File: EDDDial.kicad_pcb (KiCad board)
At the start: 2 copper layers, 49 parts, among them J1 USB_C_Receptacle_USB2.0_16P, J2 Conn_01x03_MountingPin, J3 Conn_ARM_SWD_TagConnect_TC203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, J4 Conn_01x05_MountingPin, J5 Conn_01x05_MountingPin, U1 nRF52820-QDxx, U3 WE-TVS-82400102, U4 TPS7A02DBV, U5 TMAG5173A1QDBVRQ1, U6 BQ24072RGT, Y1 32mhz, Y2 32.768khz

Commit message: primary design done, may change some minor things
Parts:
- removed C12, C15: 4.7uF, Capacitor_SMD:C_0402_1005Metric
- removed C14, C16, C18: 100nF, Capacitor_SMD:C_0402_1005Metric
- removed C17, C20: 1uF, Capacitor_SMD:C_0402_1005Metric
- removed C19: 100pF, Capacitor_SMD:C_0402_1005Metric
- removed C21: 47nF, Capacitor_SMD:C_0402_1005Metric
- removed C22: 1pF, Capacitor_SMD:C_0402_1005Metric
- removed C23: 1.2pF, Capacitor_SMD:C_0402_1005Metric
- removed D1: LED, LED_SMD:LED_0402_1005Metric
- removed L1: 10uH, Inductor_SMD:L_0402_1005Metric
- removed L2: 15nH, Inductor_SMD:L_0402_1005Metric
- removed L3: 4.7nF, Inductor_SMD:L_0402_1005Metric
- removed L4: 2.2nF, Inductor_SMD:L_0402_1005Metric
- removed U1: nRF52820-QDxx, Package_DFN_QFN:QFN-40-1EP_5x5mm_P0.4mm_EP3.6x3.6mm
- removed Y1: 32mhz, Crystal:Crystal_SMD_2012-2Pin_2.0x1.2mm
- added D2: LED, LED_SMD:LED_0402_1005Metric, F.Cu at (147.1, 52.5)
- added D3: LED, LED_SMD:LED_0402_1005Metric, F.Cu at (145.9, 54.5)
- added R11: 56k, Resistor_SMD:R_0402_1005Metric, F.Cu at (140.3, 40.2)
- added R12: 100k, Resistor_SMD:R_0402_1005Metric, F.Cu at (140.3, 42.2)
- added R13: 4.7k, Resistor_SMD:R_0402_1005Metric, F.Cu at (140.3, 44.2)
- added R14: 56k, Resistor_SMD:R_0402_1005Metric, F.Cu at (153.5, 46.3)
- added R8: 4.7k, Resistor_SMD:R_0402_1005Metric, F.Cu at (140.3, 38.3)
- added U2: MDBT50Q-1MV2, RF_Module:Raytac_MDBT50Q, F.Cu at (132.1, 46.0)
- C13: value 4.7uF -> 10uF
- C4: value 12pF -> 10uF
- C6: value 12pF -> 0.1uF
- C9: value 820pF -> 0.1uF
- R3: value 1.5k -> 10k
- moved C10 35.6 mm to (82.2, 77.8), turned to 180 degrees
- moved J4 34.5 mm to (82.5, 70.2), turned to 180 degrees
- moved Y2 32.1 mm to (129.1, 55.4), turned to 180 degrees
- moved U5 25.9 mm to (82.2, 75.6)
- moved J2 24.7 mm to (124.5, 70.7), turned to -90 degrees
- moved U6 23.8 mm to (117.0, 58.3)
- moved C6 23.2 mm to (135.1, 54.8)
- moved C7 20.0 mm to (127.1, 55.5), turned to 90 degrees
- moved C9 19.4 mm to (133.2, 54.8), turned to 180 degrees
- moved C4 19.1 mm to (133.2, 55.8)
- moved C8 18.5 mm to (131.1, 55.5), turned to 90 degrees
- moved C13 15.6 mm to (137.0, 54.8)
- moved R10 10.4 mm to (86.5, 43.6)
- moved R9 10.4 mm to (86.6, 41.6)
- moved U3 7.49 mm to (89.6, 42.6)
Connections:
- C2 pad 1: Net-(U4-VIN) -> Net-(SW1-A)
- C3 pad 1: Net-(U4-VIN) -> Net-(SW1-A)
- C4 pad 1: GND -> +3V3
- C4 pad 2: Net-(U1-XC1) -> GND
- C6 pad 1: GND -> +3V3
- C6 pad 2: Net-(U1-XC2) -> GND
- C9 pad 1: GND -> +3V3
- C9 pad 2: Net-(U1-DEC5) -> GND
- J3 pad 6: unconnected-(J3-SWO-Pad6) -> /SWO
- R3 pad 1: Net-(U4-VIN) -> Net-(SW1-B)
- R3 pad 2: Net-(D1-A) -> /CHG
- U4 pad 1: Net-(U4-VIN) -> Net-(SW1-A)
- U4 pad 3: Net-(U4-VIN) -> Net-(SW1-A)
- U6 pad 10: Net-(U4-VIN) -> Net-(SW1-B)
- U6 pad 11: Net-(U4-VIN) -> Net-(SW1-B)
- U6 pad 9: Net-(D1-K) -> /CHG
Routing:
- net VCC: track 0.00 -> 7.02 mm
- net /INT1: track 0.00 -> 5.51 mm, vias 0 -> 2
- net /SDA1: track 0.00 -> 2.82 mm
- net /SCL1: track 0.00 -> 2.66 mm
- net Net-(R10-Pad2): track 0.00 -> 1.49 mm
- net Net-(R9-Pad2): track 0.00 -> 1.37 mm
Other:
- copper layers 2 -> 4

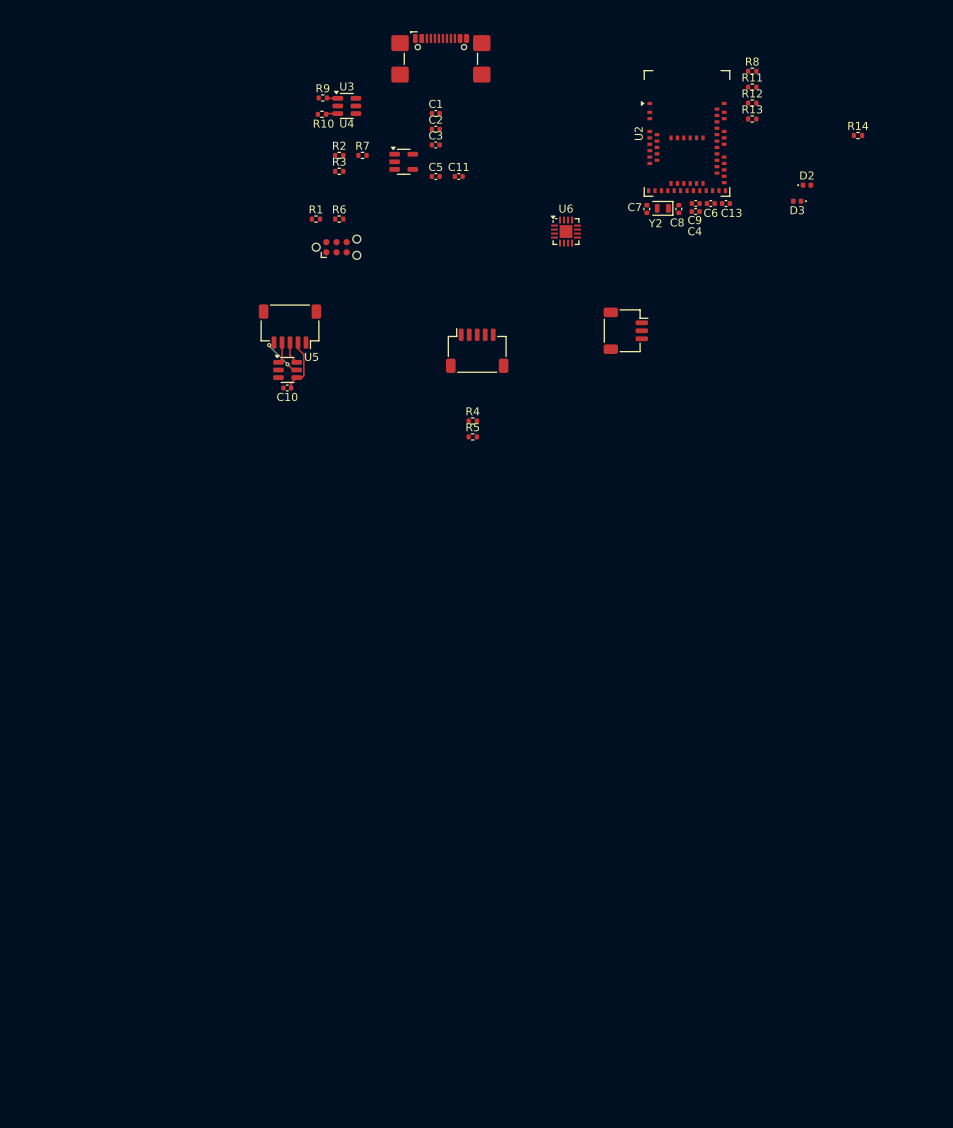
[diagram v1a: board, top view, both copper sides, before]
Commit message: Updated to be 60mm dia and completed basic routing
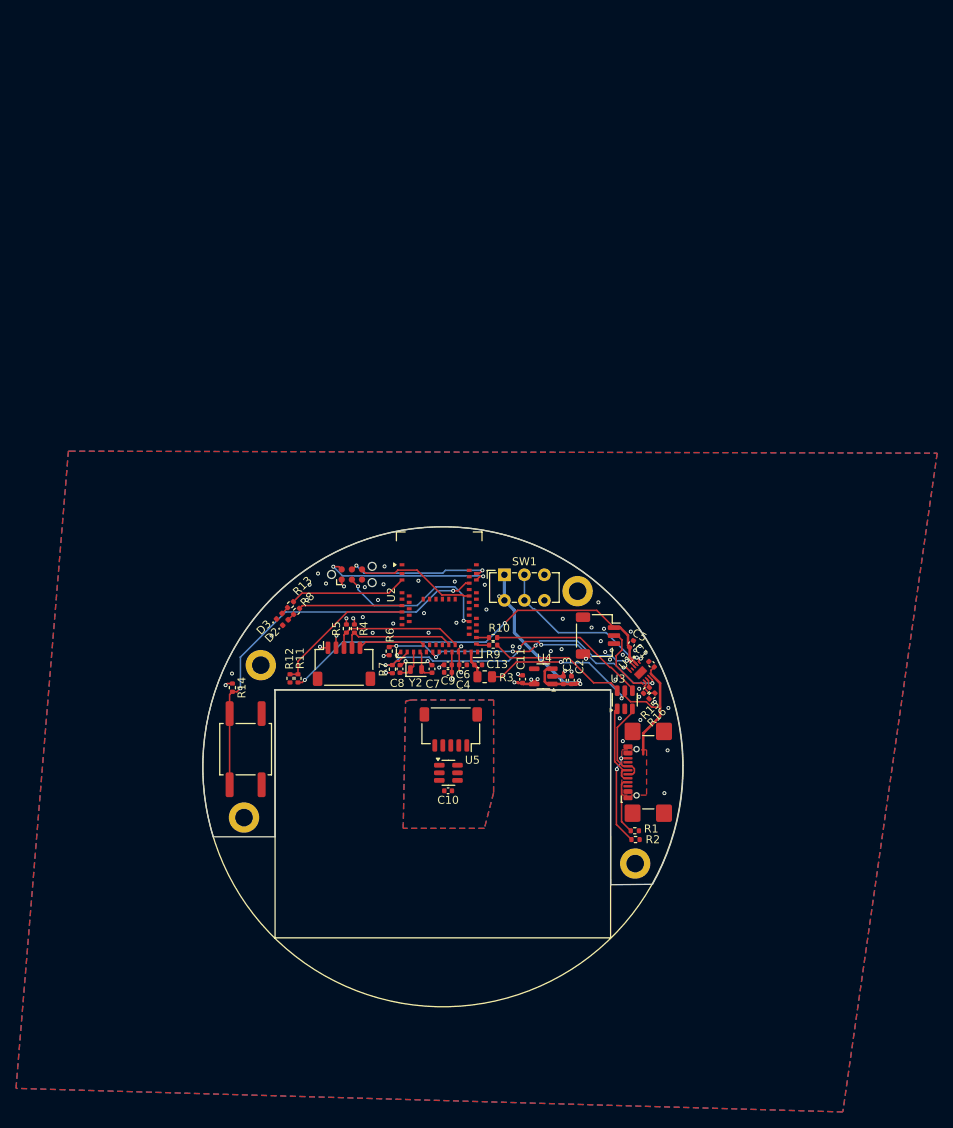
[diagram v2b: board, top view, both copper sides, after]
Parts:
- removed U6: BQ24072RGT, Package_DFN_QFN:VQFN-16-1EP_3x3mm_P0.5mm_EP1.6x1.6mm
- added H1: MountingHole_Pad, MountingHole:MountingHole_2.2mm_M2_DIN965_Pad, F.Cu at (78.8, 112.5)
- added H2: MountingHole_Pad, MountingHole:MountingHole_2.2mm_M2_DIN965_Pad, F.Cu at (76.8, 131.6)
- added H3: MountingHole_Pad, MountingHole:MountingHole_2.2mm_M2_DIN965_Pad, F.Cu at (118.5, 103.2)
- added H4: MountingHole_Pad, MountingHole:MountingHole_2.2mm_M2_DIN965_Pad, F.Cu at (125.7, 137.3)
- added R15: 1.2k, Resistor_SMD:R_0402_1005Metric, F.Cu at (127.0, 115.7)
- added R16: 18k, Resistor_SMD:R_0402_1005Metric, F.Cu at (127.8, 116.3)
- added SW1: SW_SPDT, Button_Switch_THT:SW_E-Switch_EG1271_SPDT, F.Cu at (109.3, 101.2)
- added SW2: SW_Push, Button_Switch_SMD:SW_Push_1P1T_NO_CK_KSC6xxG, F.Cu at (77.0, 123.0)
- added U1: BQ25185DLHR, FCU2025Lib:IC_BQ25185DLHR, F.Cu at (126.3, 113.4)
- R3: value 10k -> 4.7R; footprint Resistor_SMD:R_0402_1005Metric -> Resistor_SMD:R_0805_2012Metric
- R6, R7: value 3.3k -> 10k
- moved R14 104.3 mm to (75.3, 115.3), turned to -90 degrees
- moved R2 93.2 mm to (125.7, 134.3)
- moved R11 93.2 mm to (83.5, 114.2), turned to 90 degrees
- moved R12 92.2 mm to (82.5, 114.2), turned to -90 degrees
- moved J1 92.1 mm to (128.4, 125.9), turned to 90 degrees
- moved R8 88.3 mm to (83.3, 105.8), turned to 45 degrees
- moved R1 86.2 mm to (125.6, 133.2)
- moved D2 85.1 mm to (81.9, 107.2), turned to 45 degrees
- moved R13 83.8 mm to (82.6, 104.9), turned to 45 degrees
- moved D3 83.0 mm to (81.2, 106.4), turned to 45 degrees
- moved U3 82.0 mm to (124.4, 116.8), turned to 90 degrees
- moved C1 73.9 mm to (127.7, 112.4), turned to 135 degrees
- moved R9 71.6 mm to (107.9, 110.0), turned to 180 degrees
- moved C2 70.9 mm to (117.7, 114.4), turned to 90 degrees
- moved R10 68.8 mm to (107.9, 109.0), turned to 180 degrees
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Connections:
- C13 pad 1: VBUS -> Net-(U2-VBUS)
- R10 pad 1: Net-(J1-D+-PadA6) -> Net-(R10-Pad1)
- R10 pad 2: Net-(R10-Pad2) -> /USB_D+
- R3 pad 1: Net-(SW1-B) -> VBUS
- R3 pad 2: /CHG -> Net-(U2-VBUS)
- R6 pad 1: Net-(U6-ISET) -> +3V3
- R6 pad 2: GND -> /STAT2
- R7 pad 1: Net-(U6-ILIM) -> +3V3
- R7 pad 2: GND -> /STAT1
- R9 pad 1: Net-(J1-D--PadA7) -> Net-(R9-Pad1)
- R9 pad 2: Net-(R9-Pad2) -> /USB_D-
- U2 pad 16: /CHG -> /STAT1
- U2 pad 22: unconnected-(U2-P0.06-Pad22) -> /STAT2
- U2 pad 32: VBUS -> Net-(U2-VBUS)
- U3 pad 1: Net-(R9-Pad2) -> Net-(J1-D--PadA7)
- U3 pad 3: Net-(R10-Pad2) -> Net-(J1-D+-PadA6)
- U3 pad 4: /USB_D+ -> Net-(R10-Pad1)
- U3 pad 6: /USB_D- -> Net-(R9-Pad1)
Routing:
- net VBAT: track 0.00 -> 50.4 mm, vias 0 -> 2
- net /SWITCH: track 0.00 -> 49.3 mm, vias 0 -> 2
- net /STAT1: track 0.00 -> 41.8 mm, vias 0 -> 4
- net VBUS: track 0.00 -> 38.3 mm, vias 0 -> 2
- net /STAT2: track 0.00 -> 34.4 mm, vias 0 -> 5
- net Net-(SW1-A): track 0.00 -> 27.2 mm, vias 0 -> 3
- net Net-(SW1-4): track 0.00 -> 22.2 mm, vias 0 -> 2
- net /SWDIO: track 0.00 -> 21.5 mm, vias 0 -> 2
- net /NRST: track 0.00 -> 20.9 mm, vias 0 -> 2
- net Net-(R10-Pad1): track 0.00 -> 19.8 mm
- net /VDIV: track 0.00 -> 18.2 mm
- net /SWCLK: track 0.00 -> 18.0 mm, vias 0 -> 2
- net Net-(R9-Pad1): track 0.00 -> 17.5 mm
- net +3V3: track 0.00 -> 17.4 mm, vias 0 -> 13
- net /SDA: track 0.00 -> 16.7 mm
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- added copper zone on In2.Cu, net +3V3
- added copper zone on B.Cu, net GND
- added copper zone on F.Cu, net GND
- added copper zone on In1.Cu, net GND
- added copper zone on B.Cu, net GND1
- added copper zone on F.Cu, net GND1
- added copper zone on In1.Cu, net GND1
- added copper zone on F.Cu, net VBUS
- added copper zone on In2.Cu, net VCC
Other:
- board outline added: 60 x 44.7 mm

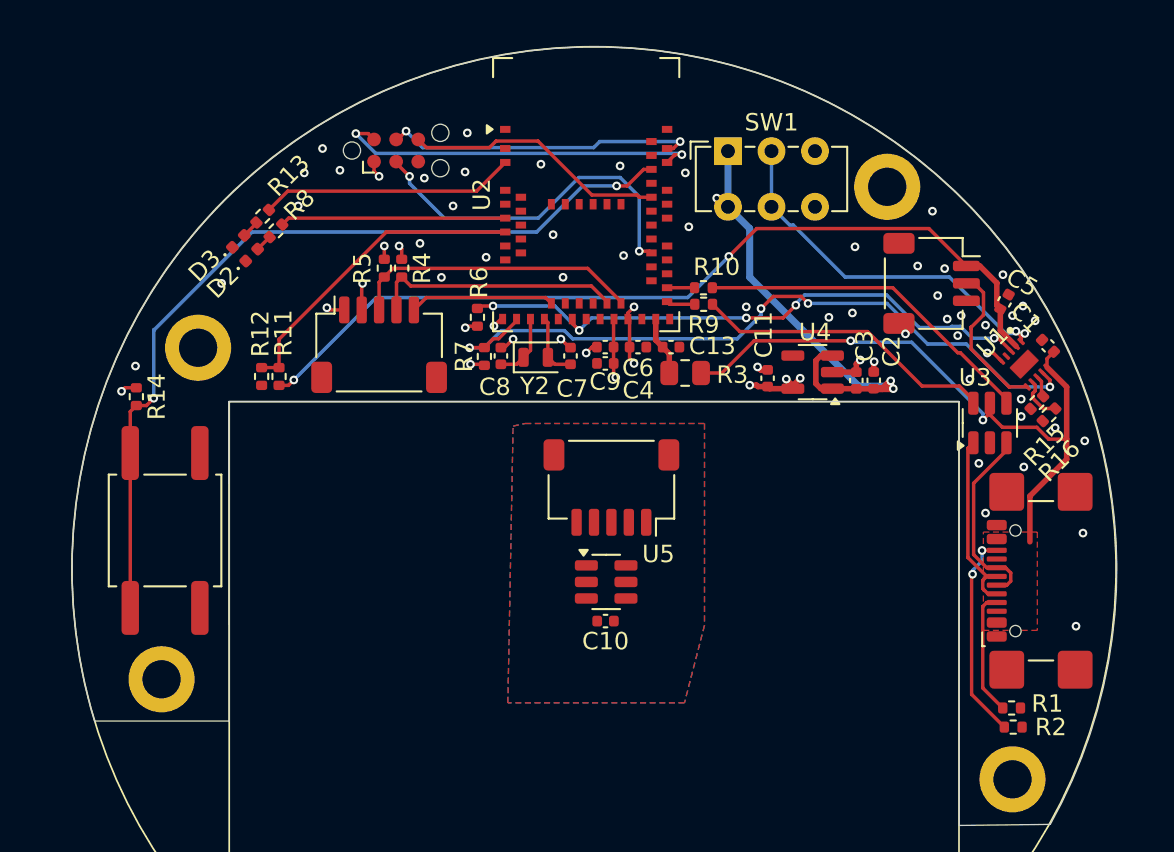
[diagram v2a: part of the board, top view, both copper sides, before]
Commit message: made 2 layer
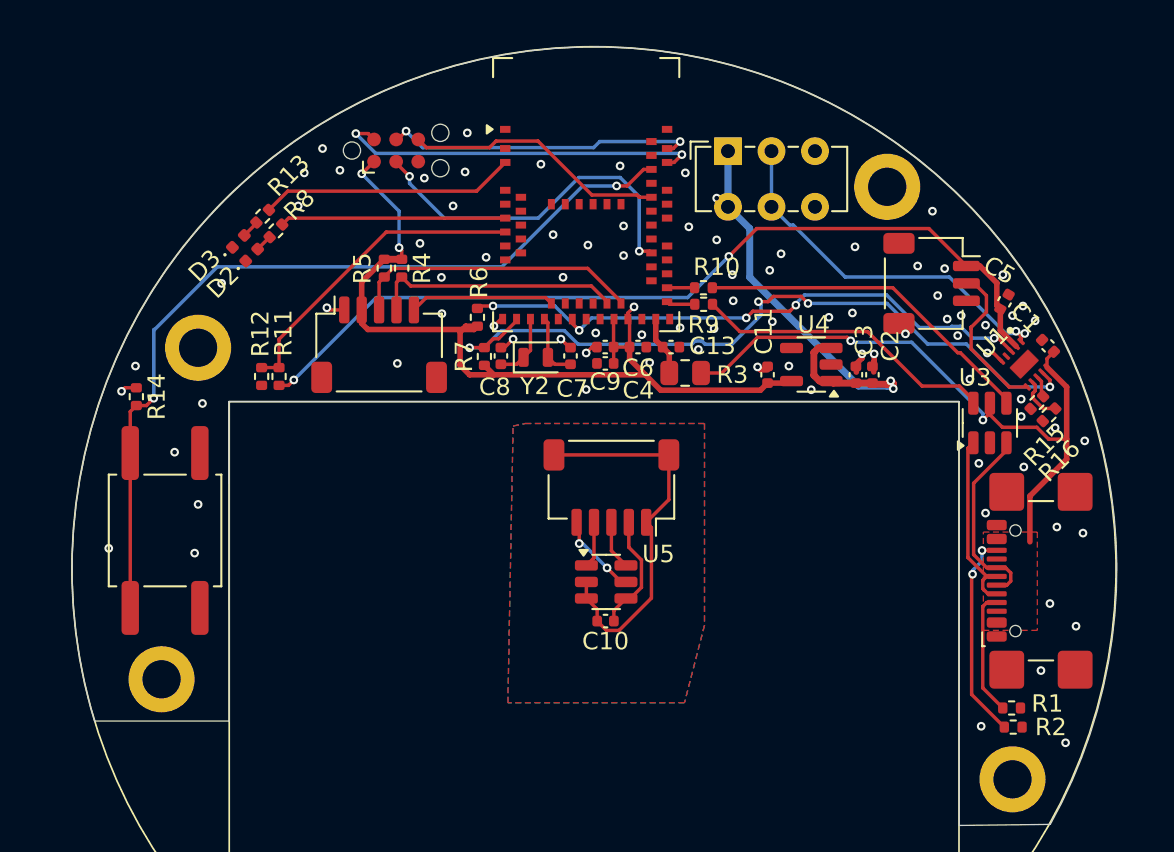
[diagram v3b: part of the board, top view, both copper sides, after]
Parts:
- moved U4 0.44 mm to (114.1, 113.5)
- moved C3 0.33 mm to (116.7, 114.0)
- moved C2 0.33 mm to (117.6, 114.0)
- moved C11 0.20 mm to (111.6, 114.0)
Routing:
- net +3V3: track 17.4 -> 51.4 mm, vias 13 -> 4
- net GND1: track 0.00 -> 22.1 mm
- net VCC: track 0.00 -> 6.78 mm
- net /INT1: track 0.00 -> 4.88 mm, vias 0 -> 2
- net /SDA1: track 0.00 -> 2.82 mm
- net /SCL1: track 0.00 -> 2.66 mm
- net /STAT1: track 41.8 -> 42.7 mm
- net GND: track 8.55 -> 8.02 mm, vias 56 -> 84

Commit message: produced device
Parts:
- added H5: MountingHole_Pad, MountingHole:MountingHole_2.2mm_M2_DIN965_Pad, F.Cu at (95.7, 120.7)
- added H6: MountingHole_Pad, MountingHole:MountingHole_2.2mm_M2_DIN965_Pad, F.Cu at (109.7, 120.7)
- added H7: MountingHole_Pad, MountingHole:MountingHole_2.2mm_M2_DIN965_Pad, F.Cu at (102.7, 132.7)
- added mouse-bite-2.54mm-slot: VAL**, Panelization:mouse-bite-2.54mm-slot, F.Cu at (102.7, 116.9)
- D2, D3: footprint LED_SMD:LED_0402_1005Metric -> LED_SMD:LED_0603_1608Metric
- moved J4 1.07 mm to (102.7, 121.6)
- moved R15 1.04 mm to (128.1, 115.8), turned to -45 degrees
- moved C10 1.00 mm to (102.7, 129.1)
- moved U5 0.90 mm to (102.7, 126.8)
- moved D3 0.71 mm to (80.5, 106.4)
- moved D2 0.54 mm to (81.5, 107.6)
- moved R16 0.42 mm to (127.3, 116.4), turned to -45 degrees
- moved R3 0.09 mm to (106.8, 113.9)
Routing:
- net GND1: track 22.1 -> 0.00 mm, vias 0 -> 4
- net +3V3: track 51.4 -> 68.3 mm
- net /SDA: track 16.7 -> 19.7 mm, vias 0 -> 2
- net /STAT1: track 42.7 -> 44.8 mm
- net VBUS: track 38.5 -> 40.6 mm
- net Net-(J1-CC2): track 12.5 -> 14.3 mm
- net /SWDIO: track 21.5 -> 23.2 mm
- net GND: track 8.02 -> 6.64 mm, vias 84 -> 82
- net /NRST: track 20.9 -> 22.1 mm
- net /STAT2: track 34.4 -> 35.5 mm
- net Net-(J1-D--PadA7): track 10.6 -> 11.3 mm
- net /INT1: track 4.88 -> 5.59 mm
- net Net-(U1-ILIM/VSET): track 2.61 -> 1.91 mm
- net Net-(SW1-4): track 22.2 -> 22.1 mm, vias 2 -> 1
- net Net-(SW1-A): track 26.7 -> 26.8 mm, vias 3 -> 2
- removed copper zone on In2.Cu, net +3V3
- removed copper zone on In1.Cu, net GND
- removed copper zone on In1.Cu, net GND1
- removed copper zone on In2.Cu, net VCC
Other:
- outline, holes or cut-outs redrawn
- copper layers 4 -> 2
- board text added: "+"
- board text added: "-"
- board text added: "1S LIPO"
- board text added: "T"
